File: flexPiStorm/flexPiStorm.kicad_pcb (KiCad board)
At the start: 2 copper layers, 32 x 103 mm, 12 parts, among them J1 Conn_01x04, J2 FPC-FFC-64, U1 MC68000

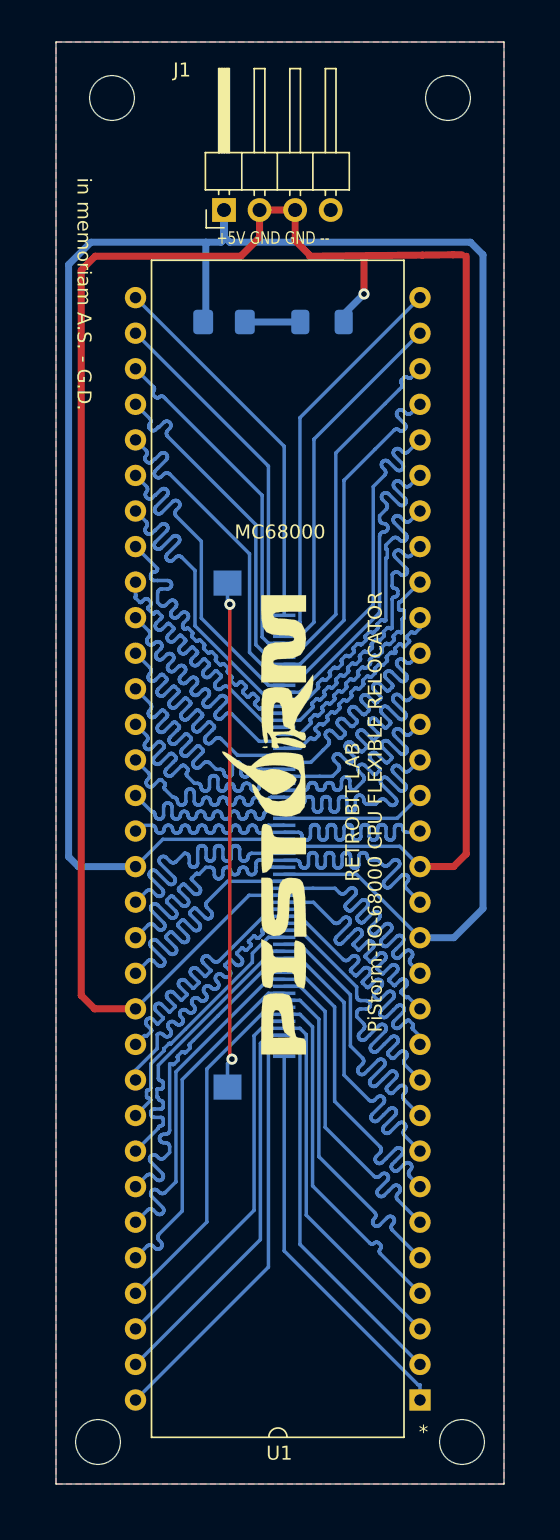
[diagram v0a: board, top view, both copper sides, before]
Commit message: Added LOGOs in the schematics, so the PCB will have them already. Run DRC for errors. Report only three (3) overlap for silkscreen and filled zones. No problem at all.
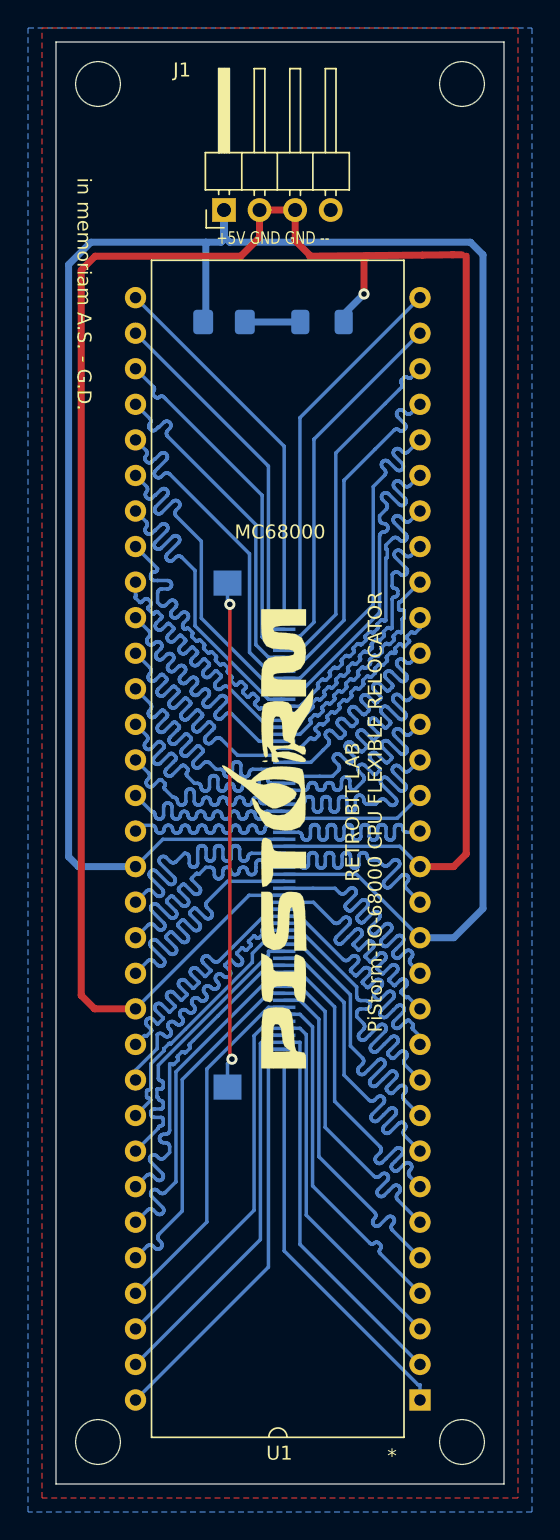
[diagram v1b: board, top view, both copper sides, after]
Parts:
- removed G***: LOGO, RetroBitLab:PiStorm_32x6-NEG
- removed REF**: Symbol_GNU-GPL_CopperTop_Small, RetroBitLab:Symbol_GNU-GPL_SilkScreen_Small
- removed REF**: KiCad-Logo2_6mm_SilkScreen, Symbol:KiCad-Logo2_6mm_SilkScreen
- added L1: GNU GPL LOGO, RetroBitLab:Symbol_GNU-GPL_SilkScreen_Small, B.Cu at (141.0, 72.0)
- added L2: KiCad LOGO Design, Symbol:KiCad-Logo2_6mm_SilkScreen, B.Cu at (141.0, 128.0)
- added L3: PiStorm LOGO Design, RetroBitLab:PiStorm_32x6-NEG, F.Cu at (140.0, 103.0)
- moved H1 1.41 mm to (128.0, 49.0)
- moved H2 1.41 mm to (154.0, 49.0)

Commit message: Added bypass capacitors 10000pF Ceramics 1206 HandSolder
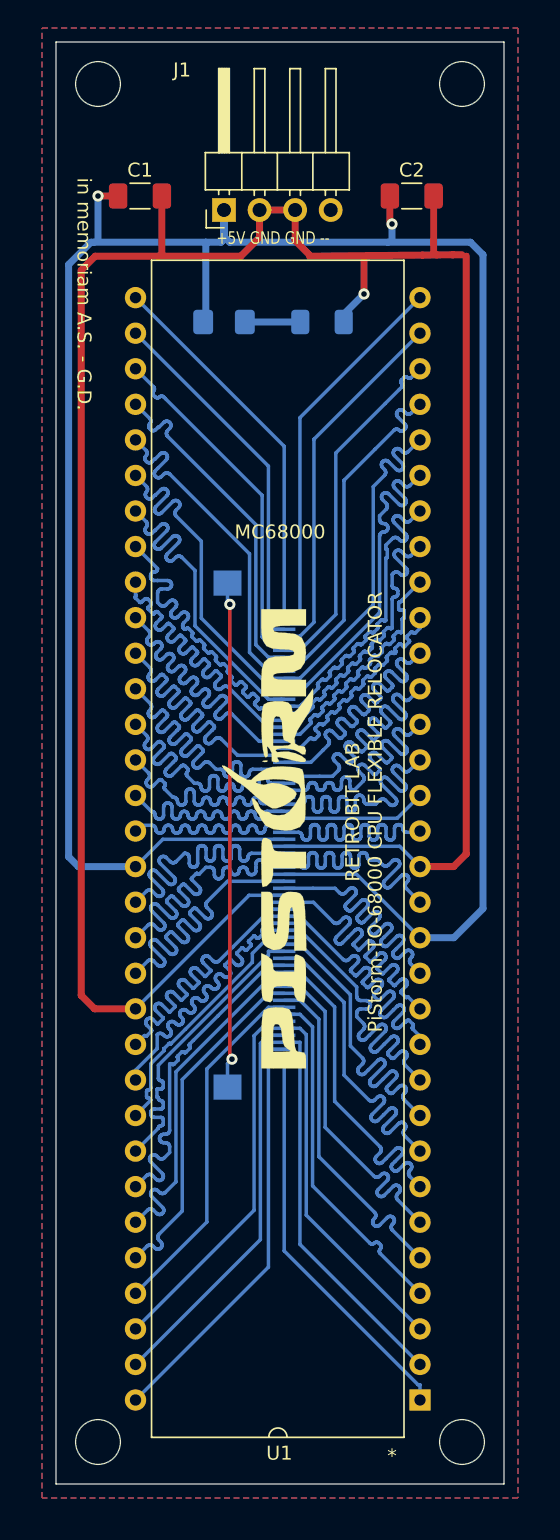
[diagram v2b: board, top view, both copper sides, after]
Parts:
- added C1: 10000pF, Capacitor_SMD:C_1206_3216Metric_Pad1.33x1.80mm_HandSolder, F.Cu at (131.0, 57.0)
- added C2: 10000pF, Capacitor_SMD:C_1206_3216Metric_Pad1.33x1.80mm_HandSolder, F.Cu at (150.4, 57.0)
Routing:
- net GND: track 169.0 -> 177.7 mm
- net VCC: track 163.1 -> 171.4 mm, vias 0 -> 2
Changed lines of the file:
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@@
     (thickness 1.6)
     (drawings 19)
-    (tracks 7760)
+    (tracks 7777)
     (zones 0)
-    (modules 12)
+    (modules 14)
     (nets 66)
   )
@@
   (title_block
     (title "Flexible CPU Seconday Relocator")
-    (date 2021-06-27)
-    (rev 0.2)
+    (date 2021-06-28)
+    (rev 0.3)
     (company "RETROBIT LAB")
     (comment 1 PiStorm)
@@
       (xy 9.008386 -0.302271)) (layer F.SilkS) (width 0.01))
   )
+  (module Capacitor_SMD:C_1206_3216Metric_Pad1.33x1.80mm_HandSolder (layer F.Cu)
+    (at 131 57)
+    (descr "Capacitor SMD 1206 (3216 Metric), square (rectangular) end terminal, IPC_7351 nominal with elongated pad for handsoldering. (Body size source: IPC-SM-782 page 76, https://www.pcb-3d.com/wordpress/wp-content/uploads/ipc-sm-782a_amendment_1_and_2.pdf), generated with kicad-footprint-generator")
+    (tags "capacitor handsolder")
+    (attr smd)
+    (fp_text reference C1 (at 0 -1.85) (layer F.SilkS)
+      (effects (font (size 1 1) (thickness 0.15)))
+    )
+    (fp_text value 10000pF (at 0 1.85) (layer F.Fab)
+      (effects (font (size 1 1) (thickness 0.15)))
+    )
+    (fp_line (start -1.6 0.8) (end -1.6 -0.8) (layer F.Fab) (width 0.1))
+    (fp_line (start -1.6 -0.8) (end 1.6 -0.8) (layer F.Fab) (width 0.1))
+    (fp_line (start 1.6 -0.8) (end 1.6 0.8) (layer F.Fab) (width 0.1))
+    (fp_line (start 1.6 0.8) (end -1.6 0.8) (layer F.Fab) (width 0.1))
+    (fp_line (start -0.711252 -0.91) (end 0.711252 -0.91) (layer F.SilkS) (width 0.12))
+    (fp_line (start -0.711252 0.91) (end 0.711252 0.91) (layer F.SilkS) (width 0.12))
+    (fp_line (start -2.48 1.15) (end -2.48 -1.15) (layer F.CrtYd) (width 0.05))
+    (fp_line (start -2.48 -1.15) (end 2.48 -1.15) (layer F.CrtYd) (width 0.05))
+    (fp_line (start 2.48 -1.15) (end 2.48 1.15) (layer F.CrtYd) (width 0.05))
+    (fp_line (start 2.48 1.15) (end -2.48 1.15) (layer F.CrtYd) (width 0.05))
+    (fp_text user %R (at 0 0) (layer F.Fab)
+      (effects (font (size 0.8 0.8) (thickness 0.12)))
+    )
+    (pad 1 smd roundrect (at -1.5625 0) (size 1.325 1.8) (layers F.Cu F.Paste F.Mask) (roundrect_rratio 0.188679)
+      (net 1 VCC))
+    (pad 2 smd roundrect (at 1.5625 0) (size 1.325 1.8) (layers F.Cu F.Paste F.Mask) (roundrect_rratio 0.188679)
+      (net 2 GND))
+    (model ${KISYS3DMOD}/Capacitor_SMD.3dshapes/C_1206_3216Metric.wrl
+      (at (xyz 0 0 0))
+      (scale (xyz 1 1 1))
+      (rotate (xyz 0 0 0))
+    )
+  )
+  (module Capacitor_SMD:C_1206_3216Metric_Pad1.33x1.80mm_HandSolder (layer F.Cu)
+    (at 150.41 57)
+    (descr "Capacitor SMD 1206 (3216 Metric), square (rectangular) end terminal, IPC_7351 nominal with elongated pad for handsoldering. (Body size source: IPC-SM-782 page 76, https://www.pcb-3d.com/wordpress/wp-content/uploads/ipc-sm-782a_amendment_1_and_2.pdf), generated with kicad-footprint-generator")
+    (tags "capacitor handsolder")
+    (attr smd)
+    (fp_text reference C2 (at 0 -1.85) (layer F.SilkS)
+      (effects (font (size 1 1) (thickness 0.15)))
+    )
+    (fp_text value 10000pF (at 0 1.85) (layer F.Fab)
+      (effects (font (size 1 1) (thickness 0.15)))
+    )
+    (fp_line (start 2.48 1.15) (end -2.48 1.15) (layer F.CrtYd) (width 0.05))
+    (fp_line (start 2.48 -1.15) (end 2.48 1.15) (layer F.CrtYd) (width 0.05))
+    (fp_line (start -2.48 -1.15) (end 2.48 -1.15) (layer F.CrtYd) (width 0.05))
+    (fp_line (start -2.48 1.15) (end -2.48 -1.15) (layer F.CrtYd) (width 0.05))
+    (fp_line (start -0.711252 0.91) (end 0.711252 0.91) (layer F.SilkS) (width 0.12))
+    (fp_line (start -0.711252 -0.91) (end 0.711252 -0.91) (layer F.SilkS) (width 0.12))
+    (fp_line (start 1.6 0.8) (end -1.6 0.8) (layer F.Fab) (width 0.1))
+    (fp_line (start 1.6 -0.8) (end 1.6 0.8) (layer F.Fab) (width 0.1))
+    (fp_line (start -1.6 -0.8) (end 1.6 -0.8) (layer F.Fab) (width 0.1))
+    (fp_line (start -1.6 0.8) (end -1.6 -0.8) (layer F.Fab) (width 0.1))
+    (fp_text user %R (at 0 0) (layer F.Fab)
+      (effects (font (size 0.8 0.8) (thickness 0.12)))
+    )
+    (pad 2 smd roundrect (at 1.5625 0) (size 1.325 1.8) (layers F.Cu F.Paste F.Mask) (roundrect_rratio 0.188679)
+      (net 2 GND))
+    (pad 1 smd roundrect (at -1.5625 0) (size 1.325 1.8) (layers F.Cu F.Paste F.Mask) (roundrect_rratio 0.188679)
+      (net 1 VCC))
+    (model ${KISYS3DMOD}/Capacitor_SMD.3dshapes/C_1206_3216Metric.wrl
+      (at (xyz 0 0 0))
+      (scale (xyz 1 1 1))
+      (rotate (xyz 0 0 0))
+    )
+  )
   (dimension 3 (width 0.15) (layer Margin)
     (gr_text "3.000 mm" (at 169.3 47.5 270) (layer Margin)
@@
   (segment (start 126.6 104.9) (end 130.68 104.9) (width 0.5) (layer B.Cu) (net 1))
   (segment (start 137 59.9) (end 137.4 60.3) (width 0.5) (layer B.Cu) (net 1))
-  (segment (start 137.4 60.3) (end 154.6 60.3) (width 0.5) (layer B.Cu) (net 1))
   (segment (start 154.6 60.3) (end 155.5 61.2) (width 0.5) (layer B.Cu) (net 1))
   (segment (start 155.5 61.2) (end 155.5 107.9) (width 0.5) (layer B.Cu) (net 1))
@@
   (segment (start 135.7 65.8125) (end 135.5125 66) (width 0.25) (layer B.Cu) (net 1))
   (segment (start 135.7 60.3) (end 135.7 65.8125) (width 0.5) (layer B.Cu) (net 1))
-  (segment (start 135.7 60.3) (end 127.5 60.3) (width 0.5) (layer B.Cu) (net 1))
   (segment (start 136.8 60.3) (end 135.7 60.3) (width 0.5) (layer B.Cu) (net 1))
+  (via (at 128 57) (size 0.8) (drill 0.4) (layers F.Cu B.Cu) (net 1))
+  (segment (start 129.4375 57) (end 128 57) (width 0.5) (layer F.Cu) (net 1))
+  (segment (start 128 60) (end 127.7 60.3) (width 0.25) (layer B.Cu) (net 1))
+  (segment (start 128 57) (end 128 60) (width 0.5) (layer B.Cu) (net 1))
+  (segment (start 135.7 60.3) (end 127.7 60.3) (width 0.5) (layer B.Cu) (net 1))
+  (segment (start 127.7 60.3) (end 127.5 60.3) (width 0.5) (layer B.Cu) (net 1))
+  (segment (start 148.8475 57) (end 148.8475 58.8475) (width 0.5) (layer F.Cu) (net 1))
+  (via (at 149 59) (size 0.8) (drill 0.4) (layers F.Cu B.Cu) (net 1))
+  (segment (start 148.8475 58.8475) (end 149 59) (width 0.25) (layer F.Cu) (net 1))
+  (segment (start 149 60) (end 148.7 60.3) (width 0.25) (layer B.Cu) (net 1))
+  (segment (start 149 59) (end 149 60) (width 0.5) (layer B.Cu) (net 1))
+  (segment (start 137.4 60.3) (end 148.7 60.3) (width 0.5) (layer B.Cu) (net 1))
+  (segment (start 148.7 60.3) (end 154.6 60.3) (width 0.5) (layer B.Cu) (net 1))
   (segment (start 141.3 106.95) (end 138.79 106.95) (width 0.25) (layer B.Cu) (net 2))
   (segment (start 138.79 106.95) (end 130.68 115.06) (width 0.25) (layer B.Cu) (net 2))
@@
   (segment (start 142.08 60.18) (end 143.1 61.2) (width 0.5) (layer F.Cu) (net 2))
   (segment (start 139.54 58) (end 142.08 58) (width 0.5) (layer F.Cu) (net 2))
-  (segment (start 151.178 61.2216) (end 153.3 61.2) (width 0.5) (layer F.Cu) (net 2))
   (segment (start 153.4 61.2) (end 153.3 61.2) (width 0.25) (layer F.Cu) (net 2))
   (segment (start 154 61.2) (end 153.4 61.2) (width 0.25) (layer F.Cu) (net 2))
@@
   (segment (start 139.54 58) (end 139.54 59.96) (width 0.5) (layer F.Cu) (net 2))
   (segment (start 139.54 59.96) (end 138.2 61.3) (width 0.5) (layer F.Cu) (net 2))
-  (segment (start 138.2 61.3) (end 127.8 61.3) (width 0.5) (layer F.Cu) (net 2))
   (segment (start 127.8 61.3) (end 126.8 62.3) (width 0.5) (layer F.Cu) (net 2))
   (segment (start 126.8 62.3) (end 126.8 114.1) (width 0.5) (layer F.Cu) (net 2))
@@
   (segment (start 143.1 61.3) (end 147.259629 61.259629) (width 0.5) (layer F.Cu) (net 2))
   (segment (start 147.259629 61.259629) (end 151.178 61.2216) (width 0.5) (layer F.Cu) (net 2))
+  (segment (start 132.5625 57) (end 132.5625 61.0375) (width 0.5) (layer F.Cu) (net 2))
+  (segment (start 132.5625 61.0375) (end 132.3 61.3) (width 0.25) (layer F.Cu) (net 2))
+  (segment (start 138.2 61.3) (end 132.3 61.3) (width 0.5) (layer F.Cu) (net 2))
+  (segment (start 132.3 61.3) (end 127.8 61.3) (width 0.5) (layer F.Cu) (net 2))
+  (segment (start 151.9725 60.9725) (end 152.211084 61.211084) (width 0.25) (layer F.Cu) (net 2))
+  (segment (start 151.9725 57) (end 151.9725 60.9725) (width 0.5) (layer F.Cu) (net 2))
+  (segment (start 151.178 61.2216) (end 152.211084 61.211084) (width 0.5) (layer F.Cu) (net 2))
+  (segment (start 152.211084 61.211084) (end 153.3 61.2) (width 0.5) (layer F.Cu) (net 2))
   (segment (start 151 143) (end 151 141.9127) (width 0.25) (layer B.Cu) (net 4))
   (segment (start 151 141.9127) (end 150.8641 141.9127) (width 0.25) (layer B.Cu) (net 4))
@@
     (polygon
       (pts
-        (xy 159 151) (xy 123 151) (xy 123 45) (xy 159 45)
+        (xy 158 150) (xy 124 150) (xy 124 45) (xy 158 45)
       )
     )

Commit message: Added a better filter for powersupply TANTALUM + CERAMIC (x2)
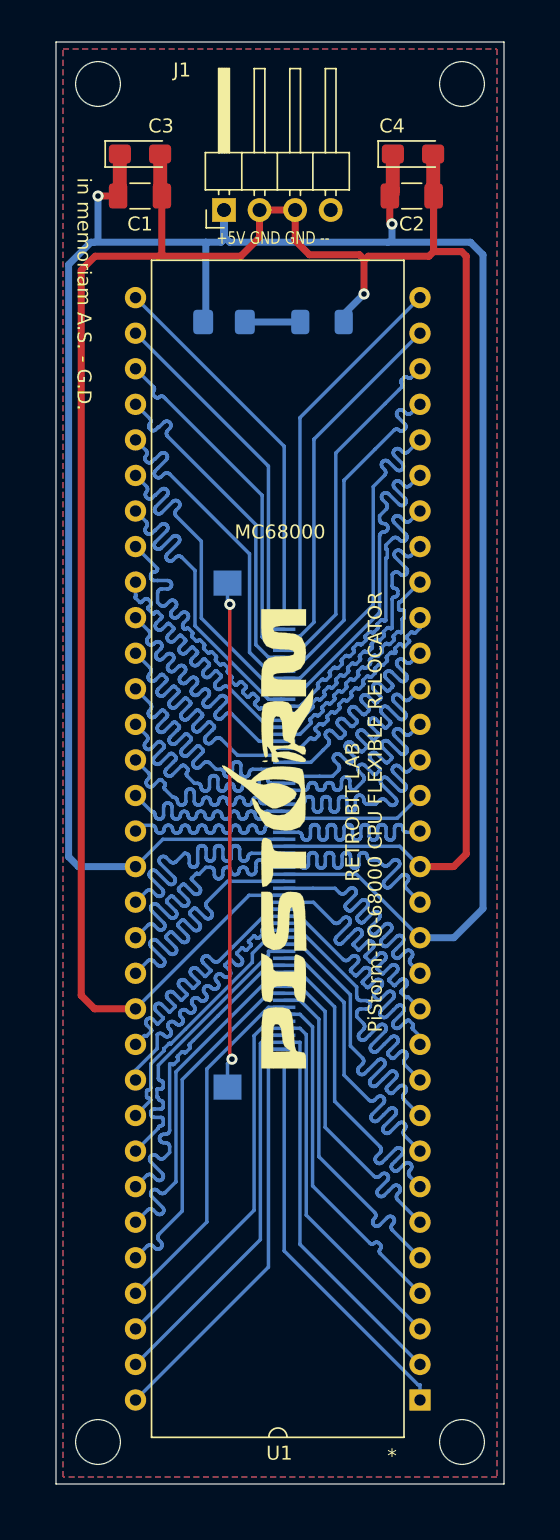
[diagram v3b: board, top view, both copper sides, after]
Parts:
- added C3: 10uF, Capacitor_Tantalum_SMD:CP_EIA-3216-12_Kemet-S_Pad1.58x1.35mm_HandSolder, F.Cu at (131.0, 54.0)
- added C4: 10uF, Capacitor_Tantalum_SMD:CP_EIA-3216-12_Kemet-S_Pad1.58x1.35mm_HandSolder, F.Cu at (150.5, 54.0)
- C1, C2: value 10000pF -> 100nF
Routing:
- net VCC: track 171.4 -> 177.6 mm
- net GND: track 177.7 -> 180.0 mm

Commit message: Modified for correct footprint CPU
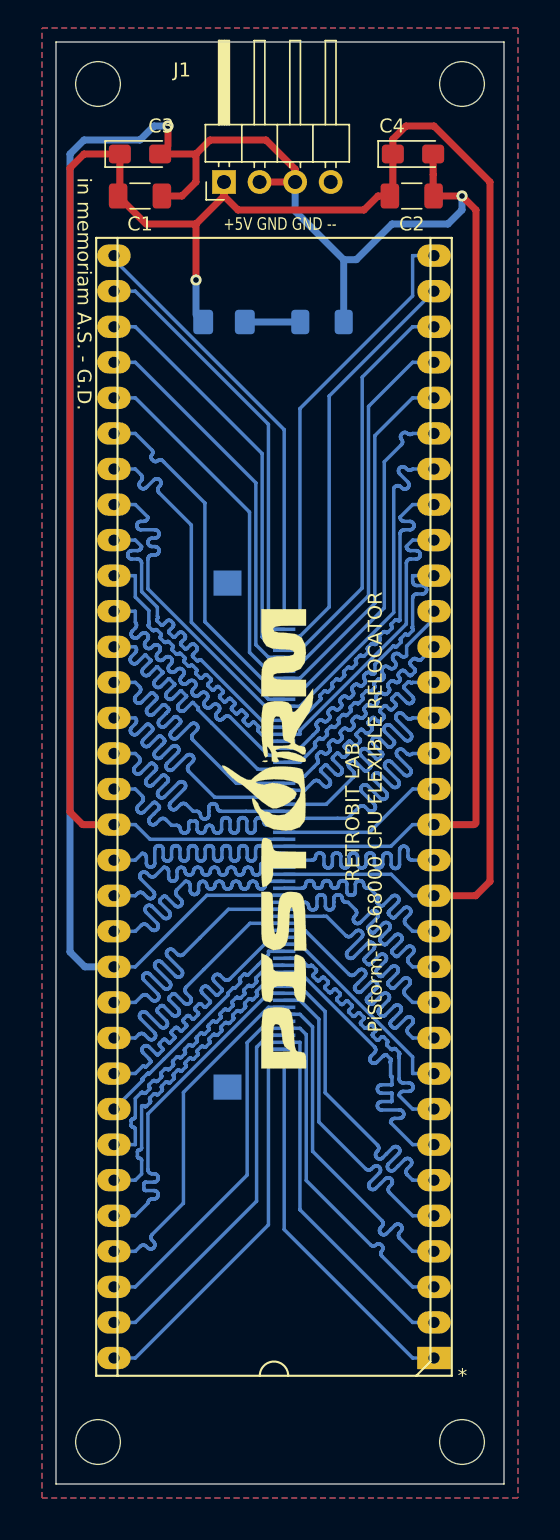
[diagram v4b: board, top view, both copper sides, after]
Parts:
- U1: footprint RetroBitLab:MC68000_REPLACEMENT_FEMALE -> RetroBitLab:MC68000-SOCKET-RELOCATOR_FEMALE
- moved U1 3.16 mm to (152.0, 140.0)
- moved J1 2.00 mm to (137.0, 56.0)
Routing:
- net Net-(J2-Pad0): track 36.3 -> 0.00 mm, vias 2 -> 0
- net /P35: track 10.4 -> 25.0 mm
- net GND: track 180.0 -> 192.6 mm, vias 1 -> 2
- net /P17: track 25.0 -> 15.2 mm
- net /P34: track 15.2 -> 23.9 mm
- net /P36: track 16.6 -> 25.0 mm
- net /P33: track 19.8 -> 12.0 mm
- net /P38: track 18.0 -> 25.0 mm
- net /P18: track 18.2 -> 25.2 mm
- net /P43: track 25.1 -> 19.1 mm
- net /P45: track 17.4 -> 22.8 mm
- net /P41: track 25.0 -> 19.8 mm
- net /P25: track 25.1 -> 19.9 mm
- net /P62: track 26.2 -> 30.7 mm
- net /P63: track 27.9 -> 32.2 mm
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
